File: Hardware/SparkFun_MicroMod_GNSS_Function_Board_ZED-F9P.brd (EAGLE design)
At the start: 37.5 x 65 mm, 163 parts, among them J1 USB Female Type C Connector, J10 455-1750-1-ND, J2 MICROMOD_FUNCTION_STANDARD, J9 U.FL, Q1 DMP21D0UT-7, U1 NLAST4501DFT2G, U10 SN74AUP1T04, U11 SN74AUP1T04, U2 3.3V, U3 EEPROM, U4 74LVC4066D_QUAD_BILATERAL_SWI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, U5 74LVC4066D_QUAD_BILATERAL_SWI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, U6 OPA344, U7 74LVC541A, U8 U-BLOX_ZED-F9P, U9 FIN1017MX

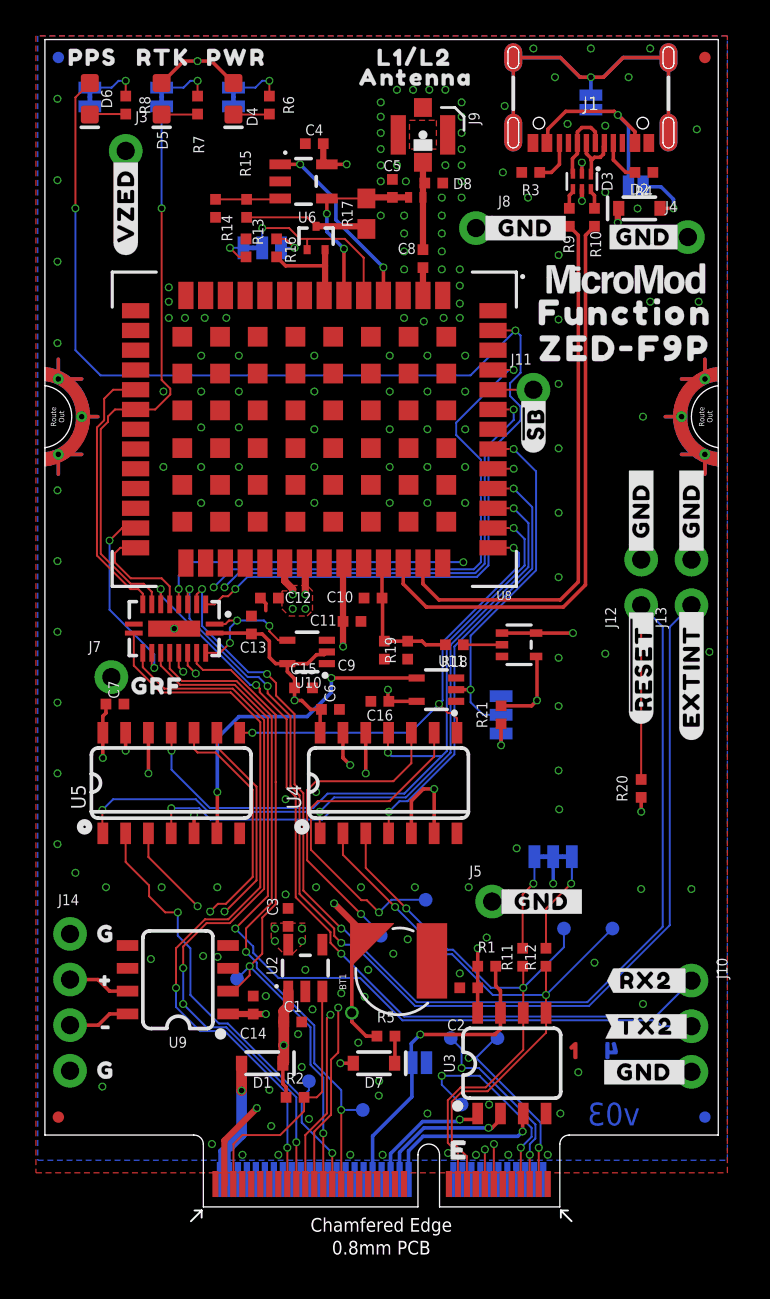
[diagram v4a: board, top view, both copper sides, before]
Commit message: Update post Reds review.
Line up USB Shield JP with CC resistors.
Relabel C8 with value, remove tolerance
Remove cap placement note.
Make USB Shield JP NC
Rename JPs to their function
Add USBSHLD Jumper text
Acid Traps
Label PPS header
Add measures
Align RST/EXTINT PTH in 0.1" grid
Move C3 back a bit from VREG
Move GND PTH back from C7
Relabel GRF as GND in silk
Recenter EXTINT AND RESET GND silk
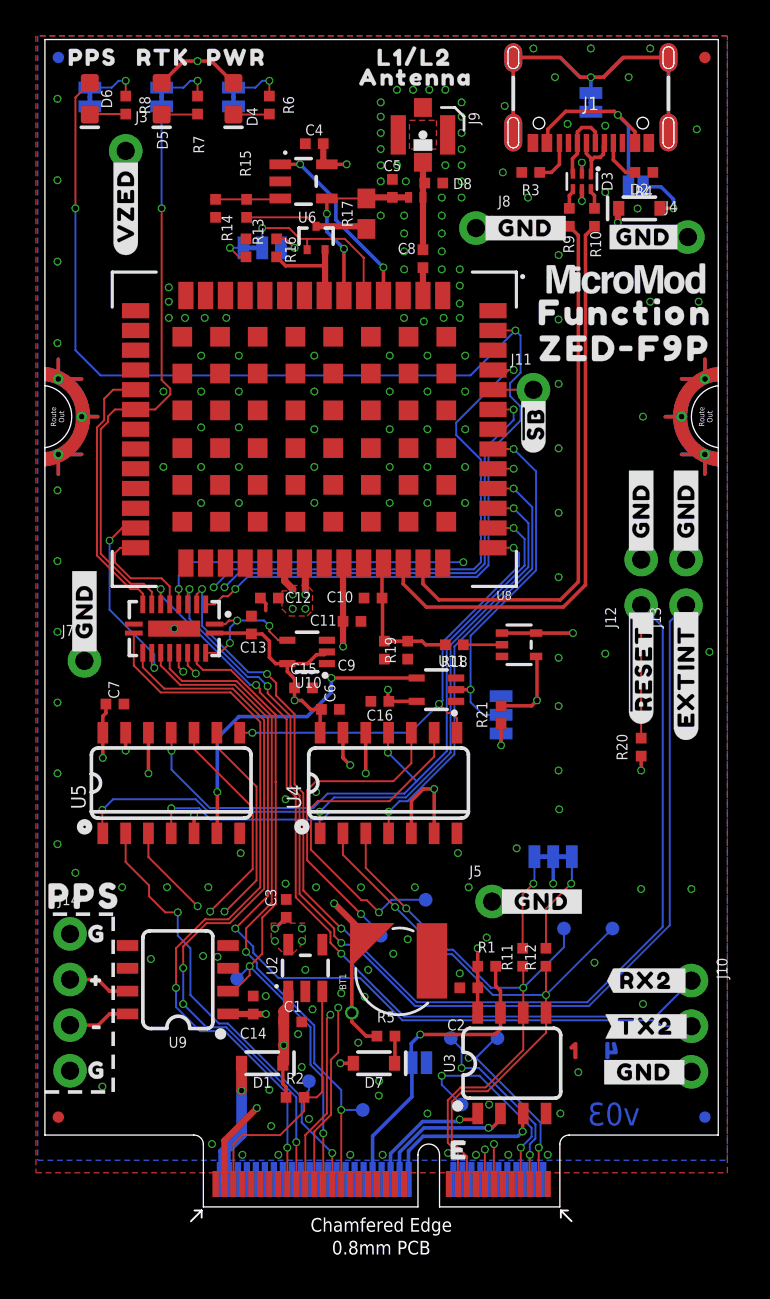
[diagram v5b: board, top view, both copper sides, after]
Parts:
- removed JP3: JUMPER-SMT_2_NO_SILK, SparkFun-Jumpers:SMT-JUMPER_2_NO_SILK
- removed U$100, U$69: (no value), output:GRF17
- added U$38, U$39: (no value), output:#_GND_#0
- added U$40: (no value), output:PPS3
- added USBSHLD: JUMPER-SMT_2_NC_TRACE_SILK, SparkFun-Jumpers:SMT-JUMPER_2_NC_TRACE_SILK
- R6, R8: value 1k -> 4.7k
- moved R20 2.30 mm to (33.2, 25.6)
- moved J7 1.75 mm to (2.20, 30.4)
- moved C3 0.51 mm to (13.4, 16.6)
- moved U$46 0.50 mm to (1.70, 15.2)
- moved U$47 0.50 mm to (1.70, 7.60)
- moved U$49 0.50 mm to (1.90, 10.0)
- moved U$48 0.50 mm to (1.80, 12.6)
- moved J13 0.30 mm to (35.7, 33.5)
- moved U$16 0.30 mm to (35.7, 33.4)
- moved U$17 0.30 mm to (35.7, 26.0)
- moved U$19 0.30 mm to (35.7, 41.3)
- moved U$22 0.30 mm to (35.7, 36.2)
- renumbered JP1 to USBPWR, JP2 to WP, JP4 to PWRLED, JP5 to RTKLED, JP6 to PPSLED, JP7 to I2CPUR, JP8 to ANTSUP, JP9 to DSEL
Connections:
- net GND: now also USBSHLD.2; no longer JP3.2
- net SHLD: now also USBSHLD.1; no longer JP3.1
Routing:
- net !RESET!: track 88.4 -> 86.1 mm
- net V_ZED: track 36.2 -> 37.1 mm
- net MM_PICO: track 45.5 -> 44.7 mm
- net ZED_RX/PICO: track 39.4 -> 38.6 mm
- net GND: vias 167 -> 169
